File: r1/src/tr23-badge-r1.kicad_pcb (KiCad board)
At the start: 4 copper layers, 111.2 x 142.3 mm, 249 parts, among them J1 532610271, J2 USB-C-12, J3 USB-A-10mm-flangeless, J4 AFC07-S40ECA-00, J5 PJ-320D, J6 2x03-socket-2.54-through-board, J7 TF-15x15, J8 DNP, Q1 MMBT3904-TP, Q2 MMBT3904-TP, Q3 MMBT3904-TP, Q4 DMG2305UX-13, Q5 DMG2305UX-13, Q6 AP2302B, SW1 REV_TACT, SW10 REV_TACT, SW11 REV_TACT, SW12 REV_TACT, SW13 REV_TACT, SW14 REV_TACT, SW15 REV_TACT, SW16 REV_TACT, SW17 REV_TACT, SW18 REV_TACT, SW19 REV_TACT, SW2 REV_TACT, SW20 REV_TACT, SW21 REV_TACT, SW22 REV_TACT, SW23 REV_TACT, SW24 REV_TACT, SW25 REV_TACT, SW26 REV_TACT, SW27 REV_TACT, SW28 REV_TACT, SW29 REV_TACT, SW3 REV_TACT, SW30 REV_TACT, SW31 REV_TACT, SW32 REV_TACT, SW33 REV_TACT, SW34 REV_TACT, SW4 REV_TACT, SW5 REV_TACT, SW6 REV_TACT, SW7 REV_TACT, SW8 REV_TACT, SW9 REV_TACT, U1 MCP73831T-2ACI_OT, U2 AP2114H-3_3TRG1, U3 CP2102N-A01-GQFN24, U4 PCM5100APW, U5 PAM8908, U6 PCA9555PW, U7 PCA9555PW, U8 PCA9555PW, U9 CC1200, Y1 32.768kHz, Y2 40Mhz

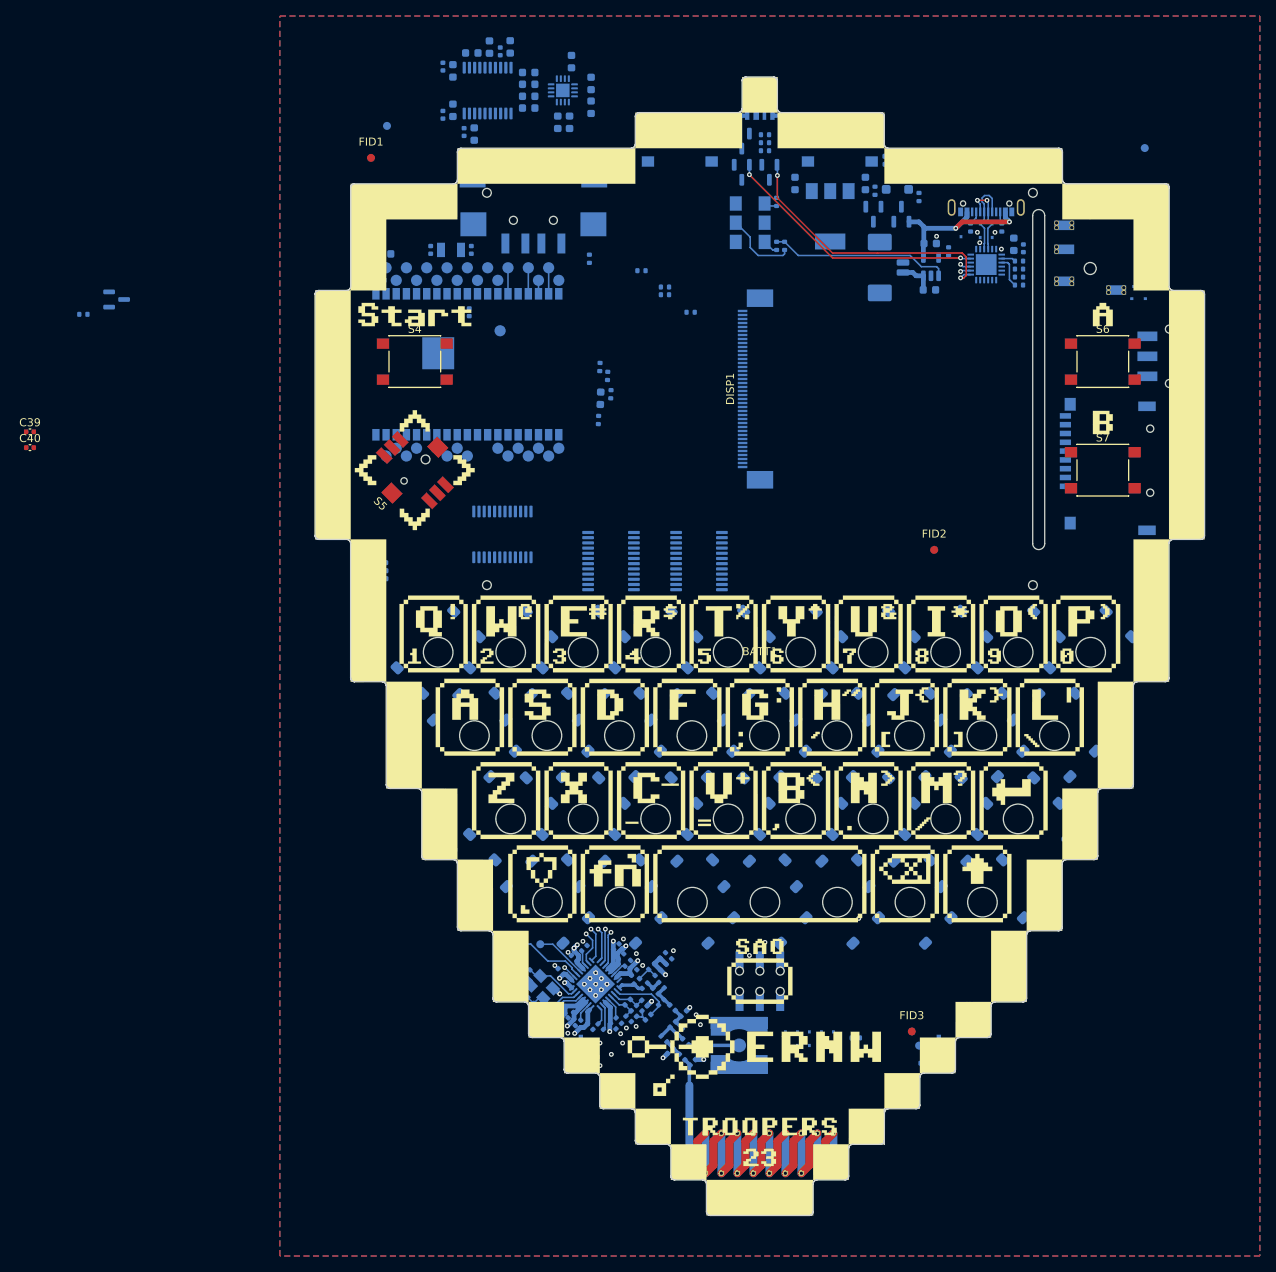
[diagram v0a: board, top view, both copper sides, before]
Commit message: First attempt at routing the keyboard
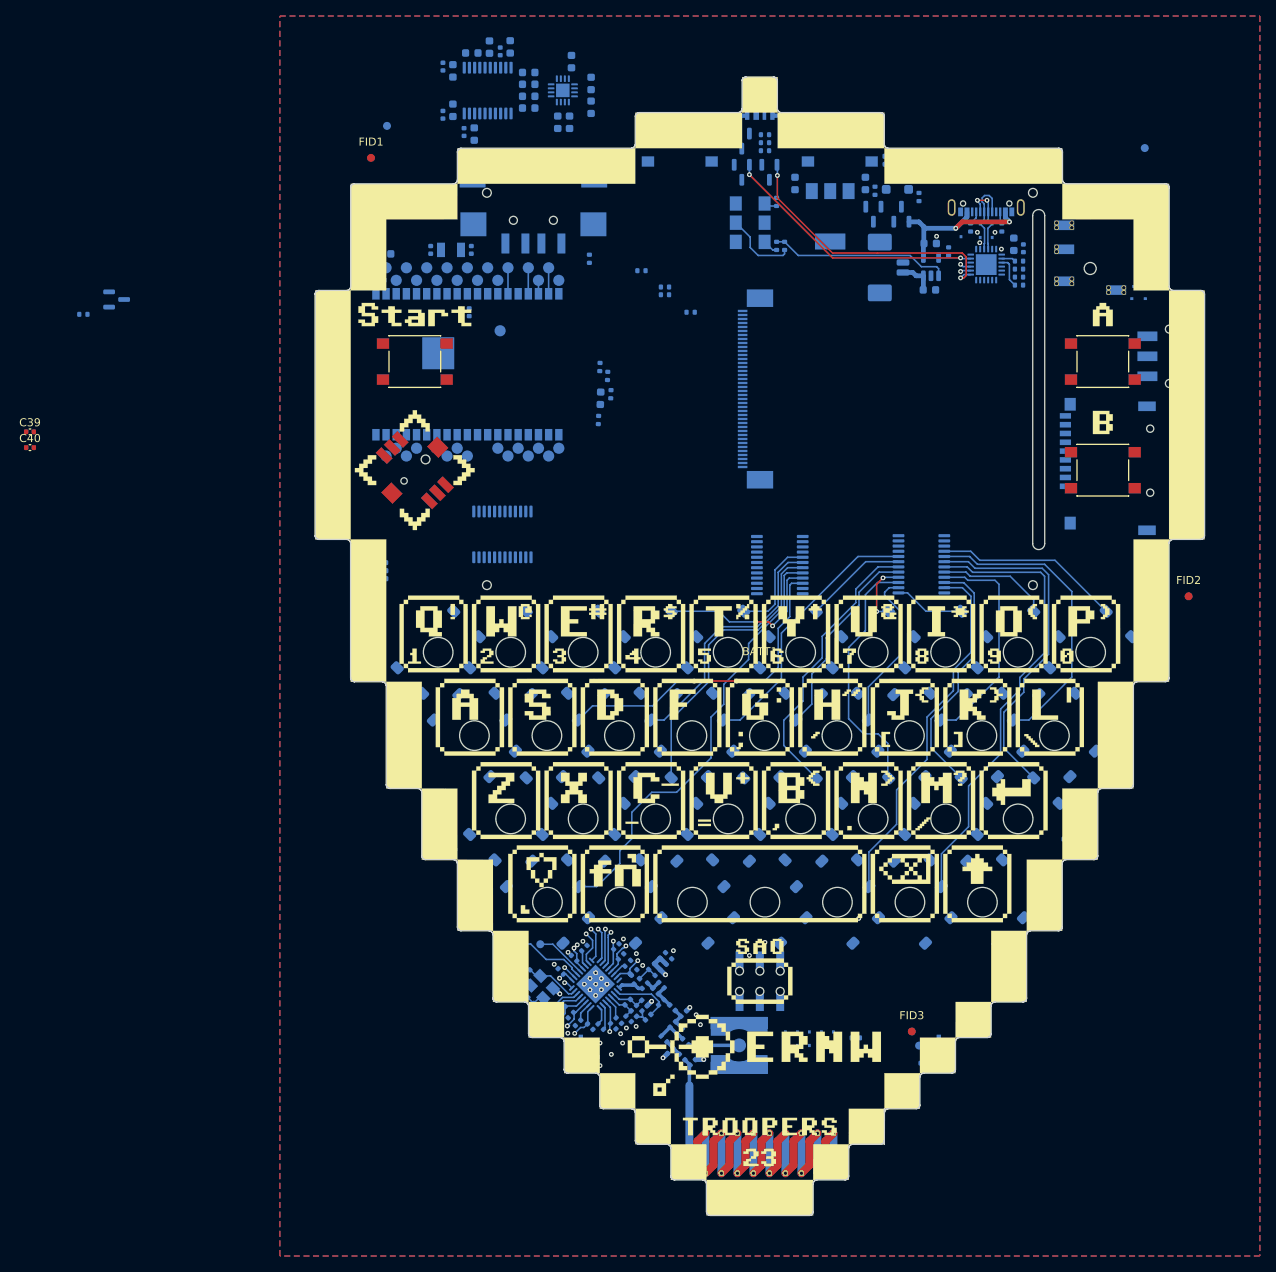
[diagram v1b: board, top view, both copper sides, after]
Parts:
- moved U7 38.8 mm to (20.2, -81.4)
- moved FID2 32.3 mm to (53.6, -77.4)
- moved U8 10.1 mm to (2.50, -81.3)
- renumbered SW10 to SW1, SW17 to SW10, SW25 to SW11, SW7 to SW12, SW16 to SW13, SW24 to SW14, SW6 to SW15, SW15 to SW16, SW23 to SW17, SW5 to SW18, SW14 to SW19, SW19 to SW2, SW22 to SW20, SW29 to SW21, SW4 to SW22, SW13 to SW23, SW21 to SW24, SW28 to SW25, SW3 to SW26, SW12 to SW27, SW20 to SW28, SW2 to SW29, SW27 to SW3, SW11 to SW30, SW1 to SW31, SW34 to SW32, SW32 to SW34, SW31 to SW4, SW9 to SW5, SW18 to SW6, SW26 to SW7, SW30 to SW8, SW8 to SW9
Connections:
- SW1 pad 3: /keyboard/KEY10 -> /keyboard/KEY0
- SW10 pad 3: /keyboard/KEY4 -> /keyboard/KEY9
- SW11 pad 3: /keyboard/KEY6 -> /keyboard/KEY10
- SW12 pad 3: /keyboard/KEY17 -> /keyboard/KEY11
- SW13 pad 3: /keyboard/KEY27 -> /keyboard/KEY12
- SW14 pad 3: /keyboard/KEY29 -> /keyboard/KEY13
- SW15 pad 3: /keyboard/KEY9 -> /keyboard/KEY14
- SW16 pad 3: /keyboard/KEY19 -> /keyboard/KEY15
- SW17 pad 3: /keyboard/KEY21 -> /keyboard/KEY16
- SW18 pad 3: /keyboard/KEY1 -> /keyboard/KEY17
- SW19 pad 3: /keyboard/KEY11 -> /keyboard/KEY18
- SW2 pad 3: /keyboard/KEY20 -> /keyboard/KEY1
- SW20 pad 3: /keyboard/KEY13 -> /keyboard/KEY19
- SW21 pad 3: /keyboard/KEY7 -> /keyboard/KEY20
- SW22 pad 3: /keyboard/KEY24 -> /keyboard/KEY21
- SW23 pad 3: /keyboard/KEY3 -> /keyboard/KEY22
- SW24 pad 3: /keyboard/KEY5 -> /keyboard/KEY23
- SW25 pad 3: /keyboard/KEY30 -> /keyboard/KEY24
- SW26 pad 3: /keyboard/KEY16 -> /keyboard/KEY25
- SW28 pad 3: /keyboard/KEY28 -> /keyboard/KEY27
- SW29 pad 3: /keyboard/KEY8 -> /keyboard/KEY28
- SW3 pad 3: /keyboard/KEY22 -> /keyboard/KEY2
- SW30 pad 3: /keyboard/KEY18 -> /keyboard/KEY29
- SW31 pad 3: /keyboard/KEY0 -> /keyboard/KEY30
- SW4 pad 3: /keyboard/KEY23 -> /keyboard/KEY3
- SW5 pad 3: /keyboard/KEY2 -> /keyboard/KEY4
- SW6 pad 3: /keyboard/KEY12 -> /keyboard/KEY5
- SW7 pad 3: /keyboard/KEY14 -> /keyboard/KEY6
- SW8 pad 3: /keyboard/KEY15 -> /keyboard/KEY7
- SW9 pad 3: /keyboard/KEY25 -> /keyboard/KEY8
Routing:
- net /keyboard/KEY3: track 0.00 -> 57.2 mm
- net /keyboard/KEY20: track 0.00 -> 55.1 mm
- net /keyboard/KEY7: track 0.00 -> 45.4 mm
- net /keyboard/KEY2: track 0.00 -> 43.0 mm
- net /keyboard/KEY22: track 0.00 -> 40.3 mm, vias 0 -> 2
- net /keyboard/KEY1: track 0.00 -> 38.0 mm
- net /keyboard/KEY19: track 0.00 -> 36.7 mm
- net /keyboard/KEY13: track 0.00 -> 35.5 mm
- net /keyboard/KEY15: track 0.00 -> 33.7 mm
- net /keyboard/KEY18: track 0.00 -> 32.2 mm
- net /keyboard/KEY10: track 0.00 -> 31.7 mm
- net /keyboard/KEY6: track 0.00 -> 31.2 mm
- net /keyboard/KEY5: track 0.00 -> 28.3 mm
- net /keyboard/KEY12: track 0.00 -> 25.2 mm
- net /keyboard/KEY0: track 0.00 -> 23.3 mm
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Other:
- board text removed: "AUDIO"
- board text removed: "Battery"
- board text removed: "Boot"
- board text removed: "IQS Debug"
- board text removed: "MicroSD"
- board text removed: "Not USB"
- board text removed: "OFF"
- board text removed: "ON"
- board text removed: "Reset"
- board text removed: "USB"
- board text removed: "rev2"

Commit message: Keyboard routed
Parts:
- moved U8 20.8 mm to (-18.2, -81.4)
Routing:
- net /keyboard/KEY31: track 0.00 -> 80.2 mm
- net /keyboard/KEY24: track 0.00 -> 41.9 mm
- net /keyboard/KEY16: track 0.00 -> 39.0 mm
- net /keyboard/KEY29: track 0.00 -> 32.6 mm
- net /keyboard/KEY27: track 0.00 -> 29.4 mm
- net /keyboard/KEY23: track 0.00 -> 27.2 mm
- net /keyboard/KEY26: track 0.00 -> 23.0 mm, vias 0 -> 2
- net /keyboard/KEY30: track 0.00 -> 20.8 mm
- net /keyboard/KEY22: track 40.3 -> 21.0 mm, vias 2 -> 0
- net /keyboard/KEY21: track 22.0 -> 7.82 mm, vias 2 -> 0
- net /keyboard/KEY1: track 38.0 -> 25.8 mm
- net /keyboard/KEY28: track 0.00 -> 11.6 mm
- net /keyboard/KEY3: track 57.2 -> 48.0 mm
- net /keyboard/KEY2: track 43.0 -> 35.9 mm, vias 0 -> 2
- net /keyboard/KEY20: track 55.1 -> 48.5 mm
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
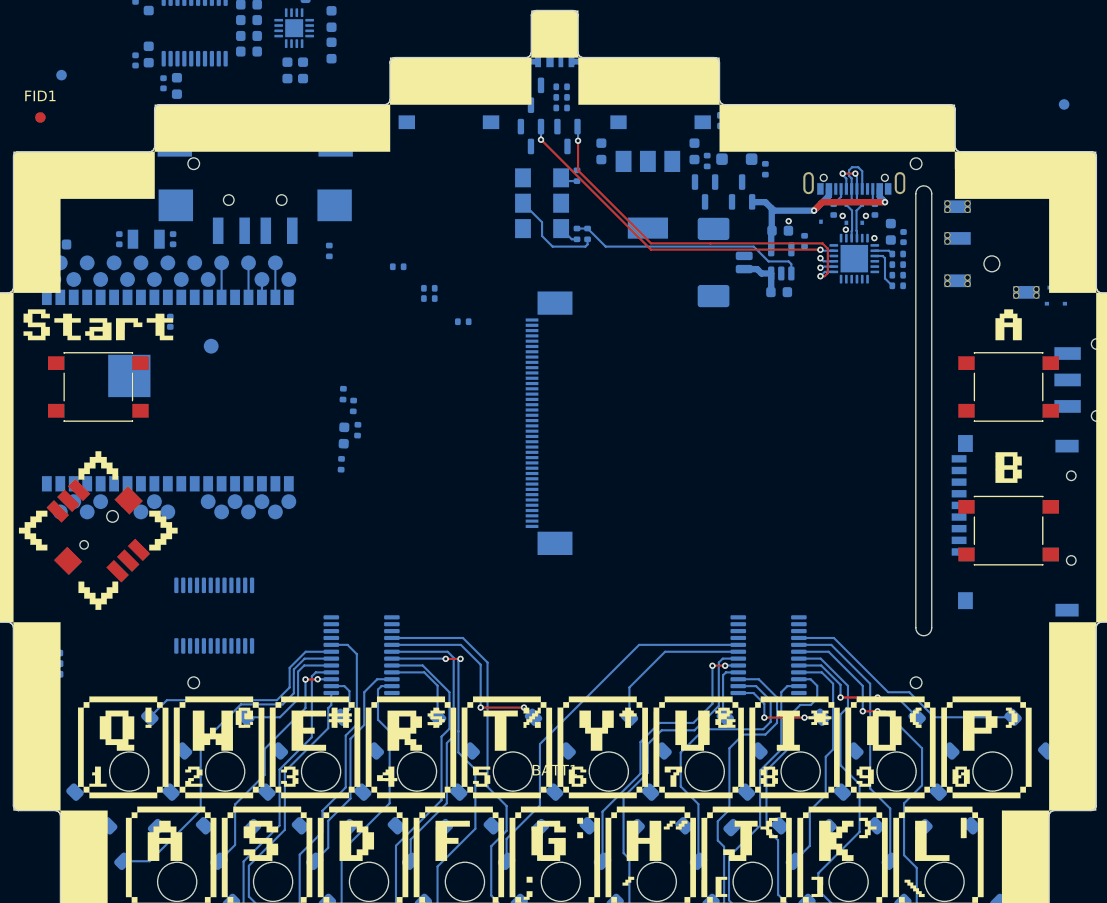
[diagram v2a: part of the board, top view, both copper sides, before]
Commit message: Rearrange power area to provide more clearance for text around rear buttons
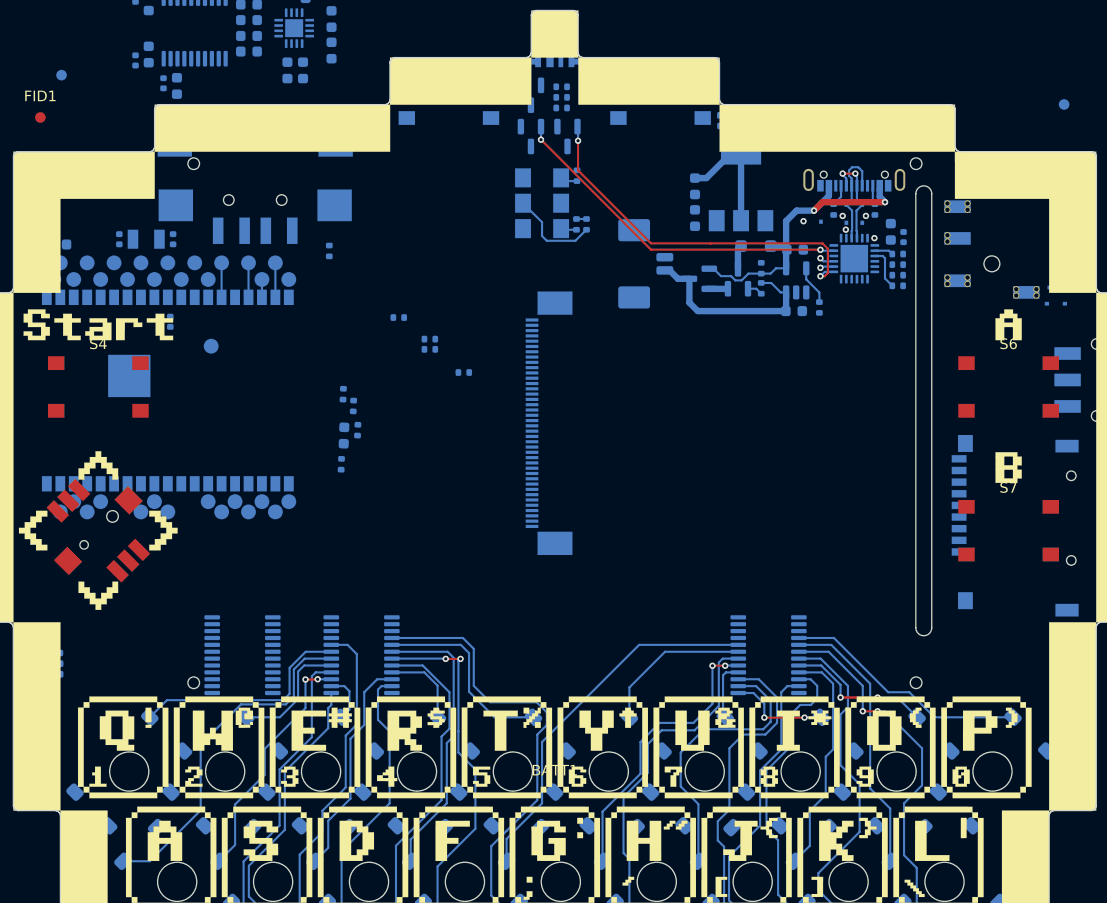
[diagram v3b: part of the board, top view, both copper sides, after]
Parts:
- S1, S2, S4, S6, S7: footprint Button_Switch_SMD:SW_SPST_PTS645 -> jeffmakes-footprints:SW_SPST_TACT-6x6-no-silk
- moved R11 13.1 mm to (19.5, -116.1)
- moved C9 9.45 mm to (13.2, -125.7)
- moved R12 9.36 mm to (19.5, -118.0), turned to 90 degrees
- moved Q4 9.14 mm to (13.7, -117.0), turned to 180 degrees
- moved U2 8.83 mm to (17.6, -125.6), turned to 90 degrees
- moved Q5 8.77 mm to (17.3, -117.0), turned to 90 degrees
- moved D3 8.41 mm to (19.0, -120.0)
- moved J1 7.50 mm to (8.00, -118.4)
- moved R8 6.41 mm to (25.0, -114.2), turned to -90 degrees
- moved C8 6.30 mm to (13.2, -122.7)
- moved R32 4.80 mm to (-8.60, -108.1)
- moved R4 4.80 mm to (-11.8, -110.3)
- moved R5 4.80 mm to (-11.8, -111.3)
- moved R6 4.80 mm to (-14.7, -113.3)
- moved U6 4.60 mm to (-29.5, -81.4), turned to 180 degrees
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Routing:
- net Net-(U1-STAT): track 22.5 -> 0.95 mm
- net +BATT: track 4.49 -> 18.8 mm
- net +3.3V: track 38.2 -> 49.8 mm
- net VBUS: track 21.3 -> 28.5 mm
- net /keyboard/KEY16: track 39.0 -> 44.7 mm
- net Net-(U1-PROG): track 0.00 -> 3.70 mm
- net +VSW: track 0.00 -> 2.27 mm
- net Net-(Q4-S): track 0.00 -> 1.77 mm
- net /power/~{PWR_EN}: track 0.00 -> 1.45 mm
- net /keyboard/KEY17: track 18.6 -> 18.3 mm, vias 2 -> 0
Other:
- board text added: "Boot"
- board text added: "Reset"
- board text removed: "tr23-outline-test-r1 2023-03-10 Monad"
